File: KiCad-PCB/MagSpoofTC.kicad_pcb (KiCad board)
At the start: 2 copper layers, 35 x 29 mm, 13 parts, among them IC1 ATTINY85-P, P1 Battery, P2 AVR ICSP, SW1 SW_PUSH, U1 TC4424

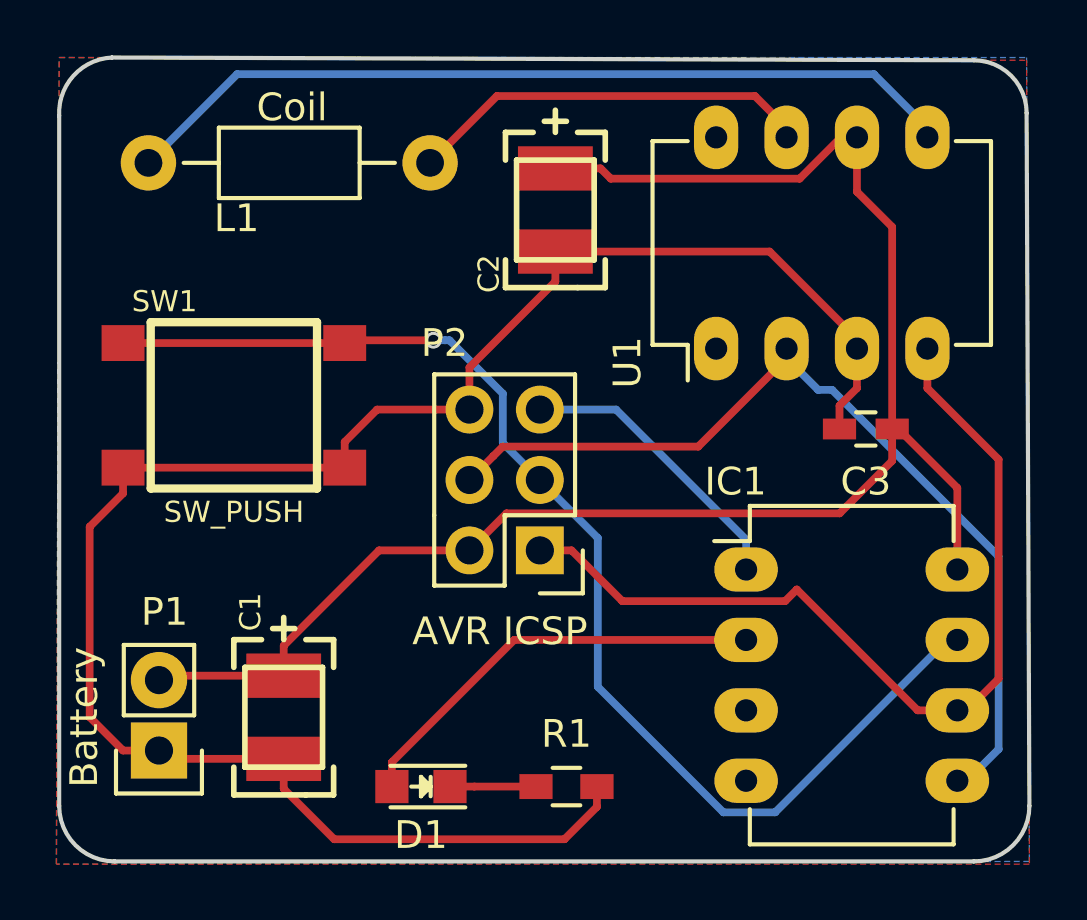
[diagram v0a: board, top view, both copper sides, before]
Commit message: Added gerber files and made vias larger for easier tools
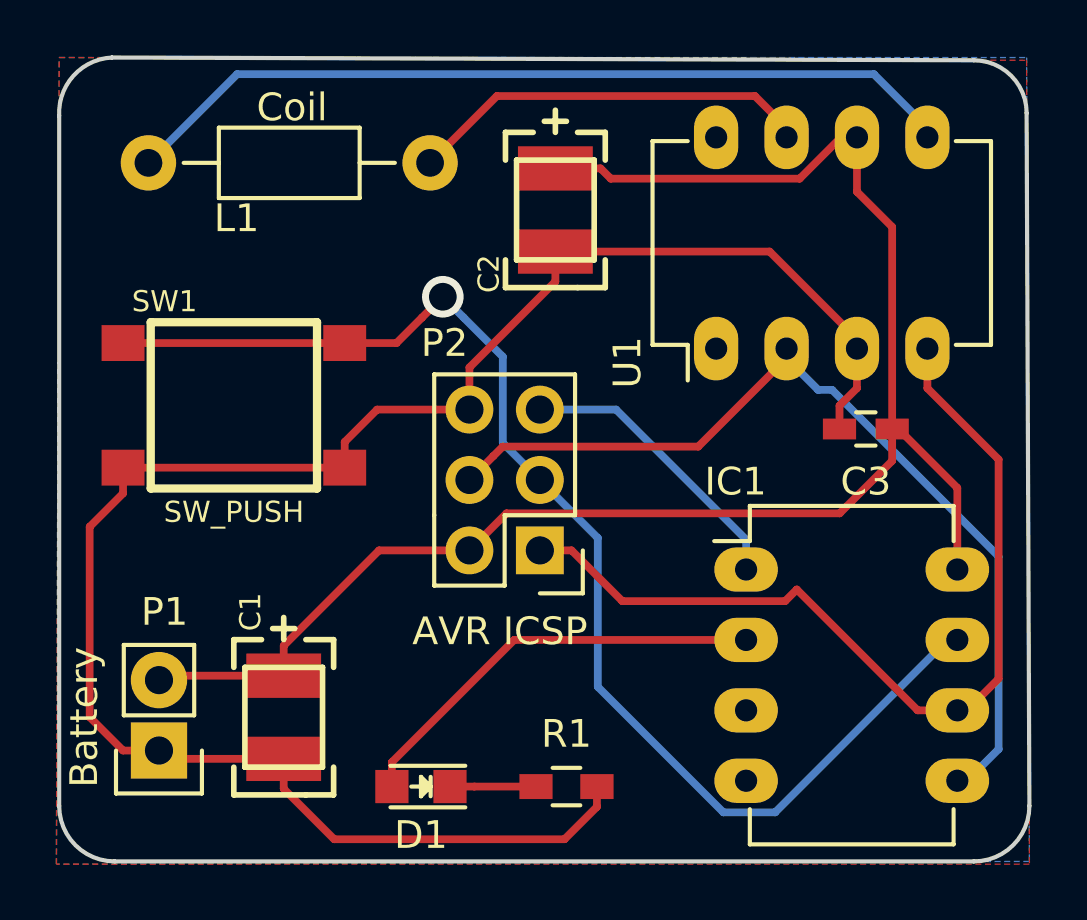
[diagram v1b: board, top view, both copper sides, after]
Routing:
- net /SCK: track 44.3 -> 46.4 mm
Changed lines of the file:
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@@
-(kicad_pcb (version 4) (host pcbnew 4.0.2+dfsg1-stable)
+(kicad_pcb (version 20171130) (host pcbnew "(5.0.1)-4")
   (general
-    (links 27)
-    (no_connects 0)
-    (area 81.102654 78.924767 138.075001 121.598481)
     (thickness 1.6)
     (drawings 11)
@@
   )
   (layers
-    (0 F.Cu signal hide)
-    (31 B.Cu signal hide)
+    (0 F.Cu signal)
+    (31 B.Cu signal)
     (32 B.Adhes user)
     (33 F.Adhes user)
     (34 B.Paste user)
     (35 F.Paste user)
-    (36 B.SilkS user)
+    (36 B.SilkS user hide)
     (37 F.SilkS user)
     (38 B.Mask user)
@@
     (mod_text_size 1 1)
     (mod_text_width 0.15)
-    (pad_size 1.524 1.524)
-    (pad_drill 0.762)
+    (pad_size 1.7272 1.7272)
+    (pad_drill 1.016)
     (pad_to_mask_clearance 0.2)
+    (solder_mask_min_width 0.25)
     (aux_axis_origin 0 0)
-    (visible_elements FFFFFF7F)
+    (visible_elements 7FFFFFFF)
     (pcbplotparams
-      (layerselection 0x010f0_80000001)
+      (layerselection 0x010f0_ffffffff)
       (usegerberextensions false)
+      (usegerberattributes false)
+      (usegerberadvancedattributes false)
+      (creategerberjobfile false)
       (excludeedgelayer true)
       (linewidth 0.100000)
@@
       (hpglpennumber 1)
       (hpglpenspeed 20)
-      (hpglpendiameter 15)
-      (hpglpenoverlay 2)
+      (hpglpendiameter 15.000000)
       (psnegative false)
       (psa4output false)
@@
       (drillshape 0)
       (scaleselection 1)
-      (outputdirectory Gerbers_magSpoof/))
+      (outputdirectory "./Gerber_magspoof/"))
   )
   (net 0 "")
@@
       (net 1 VCC))
     (model Pin_Headers.3dshapes/Pin_Header_Straight_1x02.wrl
-      (at (xyz 0 -0.05 0))
+      (offset (xyz 0 -1.269999980926514 0))
       (scale (xyz 1 1 1))
       (rotate (xyz 0 0 90))
@@
       (net 2 GND))
     (model Pin_Headers.3dshapes/Pin_Header_Straight_2x03.wrl
-      (at (xyz 0.05 -0.1 0))
+      (offset (xyz 1.269999980926514 -2.539999961853027 0))
       (scale (xyz 1 1 1))
       (rotate (xyz 0 0 90))
@@
     (at 111.2 87.9 180)
     (fp_text reference G*** (at 0 0 180) (layer B.SilkS) hide
-      (effects (font (thickness 0.3)) (justify mirror))
+      (effects (font (size 1.524 1.524) (thickness 0.3)) (justify mirror))
     )
     (fp_text value LOGO (at 0.75 0 180) (layer B.SilkS) hide
-      (effects (font (thickness 0.3)) (justify mirror))
+      (effects (font (size 1.524 1.524) (thickness 0.3)) (justify mirror))
     )
     (fp_poly (pts (xy -1.511952 -2.134469) (xy -1.457322 -2.134584) (xy -1.408721 -2.134798) (xy -1.367028 -2.135106)
@@
   (segment (start 135.4 102.55) (end 133.97 102.55) (width 0.28) (layer F.Cu) (net 8))
   (segment (start 133.97 102.55) (end 129.609999 98.189999) (width 0.28) (layer F.Cu) (net 8))
-  (segment (start 120.34 94.24) (end 119.003601 92.903601) (width 0.28) (layer B.Cu) (net 9))
-  (segment (start 119.003601 92.903601) (end 119.003601 91.122271) (width 0.28) (layer B.Cu) (net 9))
-  (segment (start 119.003601 91.122271) (end 117.08133 89.2) (width 0.28) (layer B.Cu) (net 9))
-  (segment (start 117.08133 89.2) (end 116.924264 89.2) (width 0.28) (layer B.Cu) (net 9))
-  (segment (start 116.924264 89.2) (end 116.5 89.2) (width 0.28) (layer B.Cu) (net 9))
   (segment (start 126.957793 106.23001) (end 128.82999 106.23001) (width 0.28) (layer B.Cu) (net 9))
   (segment (start 128.82999 106.23001) (end 135.05 100.01) (width 0.28) (layer B.Cu) (net 9))
   (segment (start 135.05 100.01) (end 135.4 100.01) (width 0.28) (layer B.Cu) (net 9))
-  (segment (start 116.5 89.2) (end 113.4 89.2) (width 0.28) (layer F.Cu) (net 9))
-  (segment (start 113.4 89.2) (end 113.3 89.3) (width 0.28) (layer F.Cu) (net 9))
-  (via (at 116.5 89.2) (size 0.6) (drill 0.4) (layers F.Cu B.Cu) (net 9))
   (segment (start 120.34 94.24) (end 122.42999 96.32999) (width 0.28) (layer B.Cu) (net 9))
   (segment (start 122.42999 96.32999) (end 122.42999 101.702207) (width 0.28) (layer B.Cu) (net 9))
@@
   (segment (start 105.30408 89.3) (end 106.35878 89.3) (width 0.28) (layer F.Cu) (net 9))
   (segment (start 106.35878 89.3) (end 113.3 89.3) (width 0.28) (layer F.Cu) (net 9))
+  (via (at 116.840066 87.63) (size 1.5) (drill 1) (layers F.Cu B.Cu) (net 9))
+  (segment (start 113.3 89.3) (end 115.170066 89.3) (width 0.28) (layer F.Cu) (net 9))
+  (segment (start 119.003601 89.793535) (end 117.590065 88.379999) (width 0.28) (layer B.Cu) (net 9))
+  (segment (start 117.590065 88.379999) (end 116.840066 87.63) (width 0.28) (layer B.Cu) (net 9))
+  (segment (start 119.003601 92.903601) (end 119.003601 89.793535) (width 0.28) (layer B.Cu) (net 9))
+  (segment (start 120.34 94.24) (end 119.003601 92.903601) (width 0.28) (layer B.Cu) (net 9))
+  (segment (start 116.090067 88.379999) (end 116.840066 87.63) (width 0.28) (layer F.Cu) (net 9))
+  (segment (start 115.170066 89.3) (end 116.090067 88.379999) (width 0.28) (layer F.Cu) (net 9))
   (segment (start 116.38 82.8) (end 118.79001 80.38999) (width 0.28) (layer F.Cu) (net 10))
   (segment (start 118.79001 80.38999) (end 128.09999 80.38999) (width 0.28) (layer F.Cu) (net 10))
